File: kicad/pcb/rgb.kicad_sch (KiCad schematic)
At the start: 13 parts

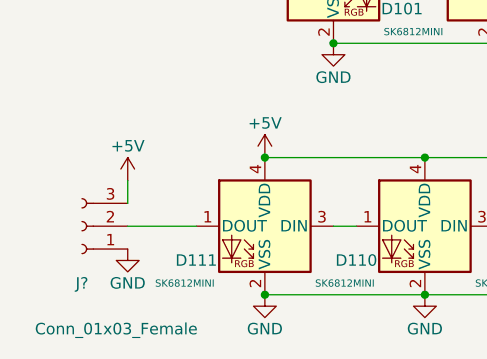
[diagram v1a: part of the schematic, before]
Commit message: fix pin order
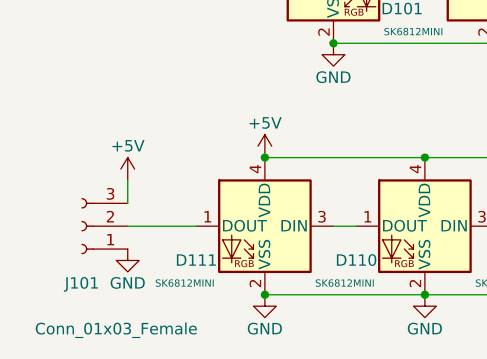
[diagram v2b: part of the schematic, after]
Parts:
- gave numbers to parts that had none: 1
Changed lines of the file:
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@@
   (symbol (lib_id "LeChiffre-rescue:Conn_01x03_Female-Connector") (at 52.07 86.36 0) (mirror y) (unit 1)
     (in_bom yes) (on_board yes) (dnp no)
-    (property "Reference" "J?" (at 52.07 92.71 0)
+    (property "Reference" "J101" (at 52.07 92.71 0)
       (effects (font (size 1.27 1.27)))
     )
@@
     (instances
       (project "stm32_hotswap_chiffre"
-        (path "/ca0d59d2-7f9b-4344-99bc-39bc2c8c88cb/9412d715-f7b7-4535-9cc7-549a2178ec10"
-          (reference "J?") (unit 1)
-        )
         (path "/ca0d59d2-7f9b-4344-99bc-39bc2c8c88cb/ec6e930e-09f1-49e7-aa49-9ca6fe61b6ec"
           (reference "J101") (unit 1)
@@
   (symbol (lib_id "power:GND") (at 90.17 93.98 0) (mirror y) (unit 1)
     (in_bom yes) (on_board yes) (dnp no)
-    (property "Reference" "#PWR?" (at 90.17 100.33 0)
+    (property "Reference" "#PWR0106" (at 90.17 100.33 0)
       (effects (font (size 1.27 1.27)) hide)
     )
@@
     (instances
       (project "stm32_hotswap_chiffre"
-        (path "/ca0d59d2-7f9b-4344-99bc-39bc2c8c88cb/9412d715-f7b7-4535-9cc7-549a2178ec10"
-          (reference "#PWR?") (unit 1)
-        )
         (path "/ca0d59d2-7f9b-4344-99bc-39bc2c8c88cb/ec6e930e-09f1-49e7-aa49-9ca6fe61b6ec"
           (reference "#PWR0106") (unit 1)
@@
   (symbol (lib_id "power:GND") (at 57.15 88.9 0) (mirror y) (unit 1)
     (in_bom yes) (on_board yes) (dnp no)
-    (property "Reference" "#PWR?" (at 57.15 95.25 0)
+    (property "Reference" "#PWR0105" (at 57.15 95.25 0)
       (effects (font (size 1.27 1.27)) hide)
     )
@@
     (instances
       (project "stm32_hotswap_chiffre"
-        (path "/ca0d59d2-7f9b-4344-99bc-39bc2c8c88cb/9412d715-f7b7-4535-9cc7-549a2178ec10"
-          (reference "#PWR?") (unit 1)
-        )
         (path "/ca0d59d2-7f9b-4344-99bc-39bc2c8c88cb/ec6e930e-09f1-49e7-aa49-9ca6fe61b6ec"
           (reference "#PWR0105") (unit 1)
@@
   (symbol (lib_id "power:GND") (at 80.01 66.04 0) (mirror y) (unit 1)
     (in_bom yes) (on_board yes) (dnp no)
-    (property "Reference" "#PWR?" (at 80.01 72.39 0)
+    (property "Reference" "#PWR0102" (at 80.01 72.39 0)
       (effects (font (size 1.27 1.27)) hide)
     )
@@
     (instances
       (project "stm32_hotswap_chiffre"
-        (path "/ca0d59d2-7f9b-4344-99bc-39bc2c8c88cb/9412d715-f7b7-4535-9cc7-549a2178ec10"
-          (reference "#PWR?") (unit 1)
-        )
         (path "/ca0d59d2-7f9b-4344-99bc-39bc2c8c88cb/ec6e930e-09f1-49e7-aa49-9ca6fe61b6ec"
           (reference "#PWR0102") (unit 1)
@@
   (symbol (lib_id "power:GND") (at 72.39 93.98 0) (mirror y) (unit 1)
     (in_bom yes) (on_board yes) (dnp no)
-    (property "Reference" "#PWR?" (at 72.39 100.33 0)
+    (property "Reference" "#PWR020" (at 72.39 100.33 0)
       (effects (font (size 1.27 1.27)) hide)
     )
@@
     (instances
       (project "stm32_hotswap_chiffre"
-        (path "/ca0d59d2-7f9b-4344-99bc-39bc2c8c88cb/9412d715-f7b7-4535-9cc7-549a2178ec10"
-          (reference "#PWR?") (unit 1)
-        )
         (path "/ca0d59d2-7f9b-4344-99bc-39bc2c8c88cb/ec6e930e-09f1-49e7-aa49-9ca6fe61b6ec"
           (reference "#PWR020") (unit 1)
